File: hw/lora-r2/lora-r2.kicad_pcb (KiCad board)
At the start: 2 copper layers, 74 x 59 mm, 18 parts, among them J1 Conn_Coaxial, J2 SWD, J3 Conn_02x08_Odd_Even, J4 Conn_01x06, Q1 IRLML6401, U1 Pico_1_PCB, U3 MCP1700x-330xxTT

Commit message: Making progress on layout
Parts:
- removed C5: 10u, Capacitor_SMD:CP_Elec_4x5.4
- removed J4: Conn_01x06, Connector_PinHeader_2.54mm:PinHeader_1x06_P2.54mm_Vertical
- added C1: 10u, Capacitor_SMD:C_0805_2012Metric_Pad1.18x1.45mm_HandSolder, F.Cu at (80.0, 97.5)
- J3: value Conn_02x08_Odd_Even -> Conn_02x12_Odd_Even; footprint Connector_PinHeader_2.54mm:PinHeader_2x08_P2.54mm_Vertical -> Connector_PinHeader_2.54mm:PinHeader_2x12_P2.54mm_Vertical
- moved R4 56.5 mm to (73.5, 88.0)
- moved R5 56.5 mm to (73.5, 90.5)
- moved C2 56.2 mm to (80.0, 87.8), turned to 90 degrees
- moved U3 52.5 mm to (80.0, 93.9), turned to 90 degrees
- moved R1 50.2 mm to (80.0, 79.0)
- moved R2 50.2 mm to (80.0, 81.5)
- moved H3 16.0 mm to (122.0, 81.0)
- moved H4 16.0 mm to (122.0, 132.0)
- moved J2 3.58 mm to (102.9, 133.0)
- moved U1 3.50 mm to (105.6, 103.4)
- moved H1 2.83 mm to (72.0, 81.0)
- moved J3 1.39 mm to (86.0, 79.9)
- moved J1 1.08 mm to (73.5, 106.5)
- moved U2 0.70 mm to (87.6, 124.7)
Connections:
- C2 pad 1: VCONV -> VCON
- J3 pad 1: GPIO0 -> VPAN
- J3 pad 10: GPIO9 -> GPIO4
- J3 pad 11: VPAN_SENSE -> VCON_SENSE
- J3 pad 12: GPIO26 -> GPIO5
- J3 pad 13: VCON_SENSE -> GPIO27
- J3 pad 14: GPIO27 -> GPIO6
- J3 pad 15: GND -> VPAN_SENSE
- J3 pad 16: GND -> GPIO7
- J3 pad 2: GPIO1 -> GPIO0
- J3 pad 3: GPIO2 -> VPAN
- J3 pad 4: GPIO3 -> GPIO1
- J3 pad 5: GPIO4 -> VCON
- J3 pad 6: GPIO5 -> GPIO2
- J3 pad 7: GPIO6 -> +3.3V
- J3 pad 8: GPIO7 -> GPIO3
- J3 pad 9: GPIO8 -> GPIO26
- Q1 pad 1: GPIO20 -> GPIO15
- U1 pad 20: unconnected-(U1-GPIO15-Pad20) -> GPIO15
- U1 pad 26: GPIO20 -> unconnected-(U1-GPIO20-Pad26)
- U3 pad 2: +3V3 -> +3.3V
- U3 pad 3: VCONV -> VCON
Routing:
- net +3.3V: track 0.00 -> 32.7 mm
- net VCON: track 0.00 -> 17.5 mm
- net GPIO8: track 23.7 -> 10.0 mm
- net GPIO15: track 0.00 -> 11.9 mm
- net GPIO9: track 21.8 -> 10.0 mm
- net GPIO6: track 21.3 -> 10.0 mm
- net Net-(J1-In): track 0.00 -> 11.0 mm
- net GPIO7: track 19.8 -> 10.0 mm
- net GPIO4: track 18.1 -> 8.99 mm
- net GPIO2: track 17.0 -> 8.99 mm
- net VPAN: track 0.00 -> 7.88 mm
- net GPIO0: track 15.6 -> 8.70 mm
- net GPIO5: track 15.6 -> 8.99 mm
- net GPIO3: track 15.1 -> 8.99 mm
- net GPIO1: track 12.5 -> 8.50 mm
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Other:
- board size 74 x 59 mm -> 58 x 59 mm

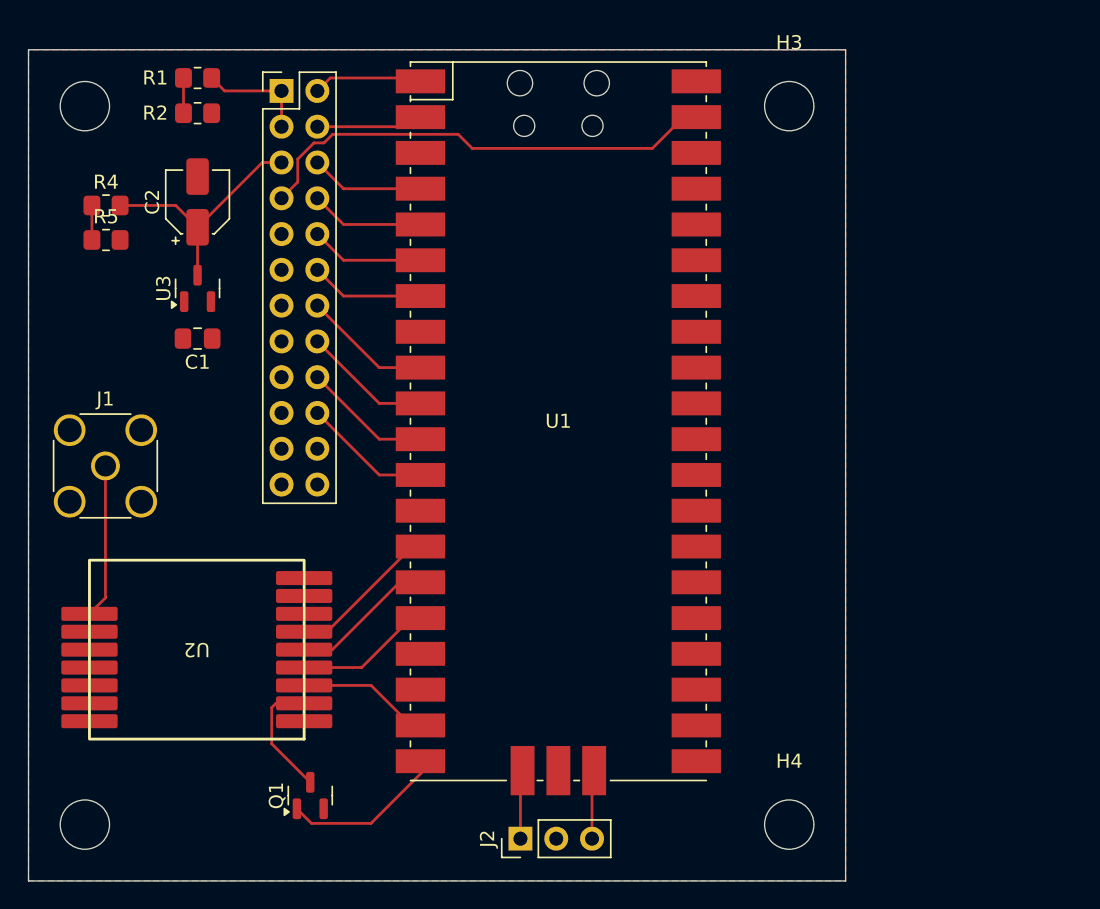
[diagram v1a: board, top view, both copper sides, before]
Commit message: First layout that passes DRC
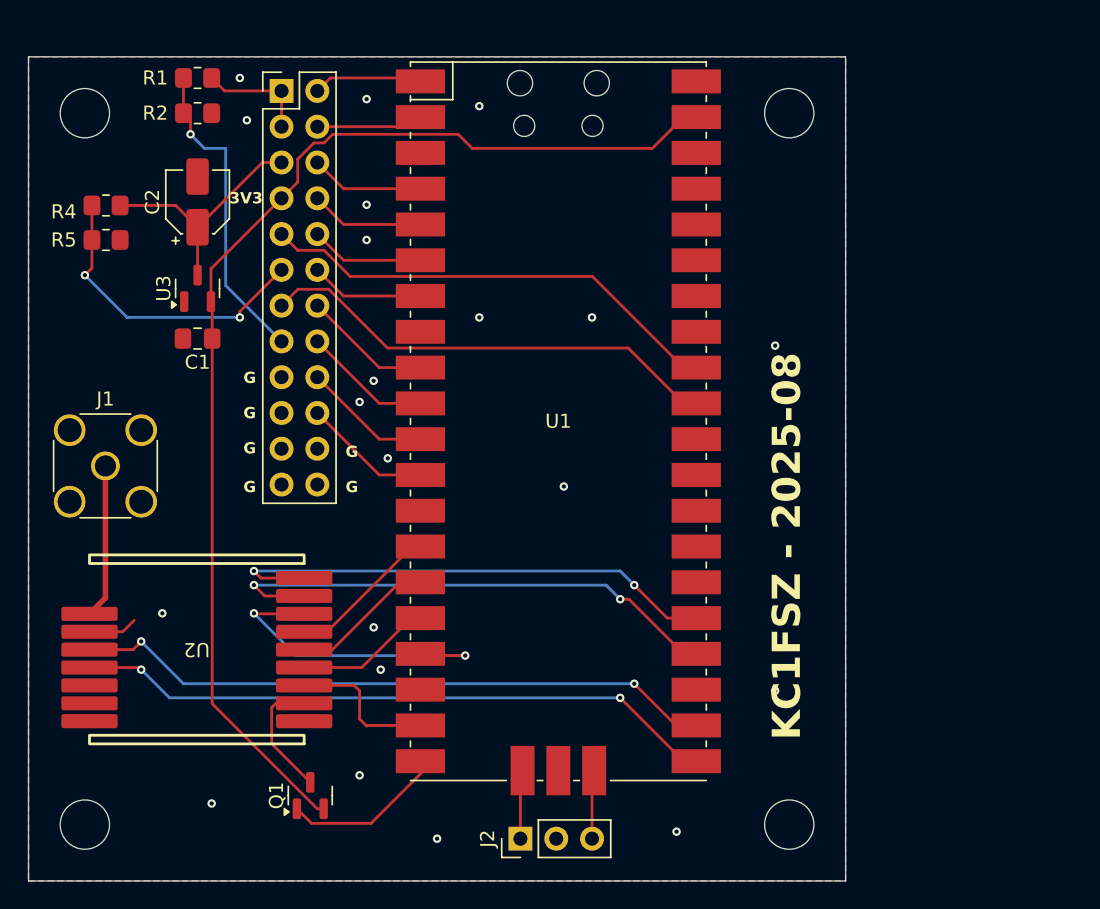
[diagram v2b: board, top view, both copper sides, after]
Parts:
- moved H1 0.50 mm to (72.0, 81.5)
- moved H3 0.50 mm to (122.0, 81.5)
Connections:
- net Net-(J1-In) renamed /Controller/ANT
- J3 pad 13: GPIO27 -> GPIO26
- J3 pad 9: GPIO26 -> GPIO27
- U1 pad 21: RADIO_RFSW_V1 -> RADIO_INT
- U1 pad 22: RADIO_RFSW_V2 -> RADIO_BUSY
- U1 pad 24: RADIO_BUSY -> RADIO_RFSW_V2
- U1 pad 25: RADIO_INT -> RADIO_RFSW_V1
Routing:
- net +3.3V: track 32.7 -> 81.7 mm
- net RADIO_INT: track 0.00 -> 44.9 mm, vias 0 -> 2
- net RADIO_BUSY: track 0.00 -> 44.9 mm, vias 0 -> 2
- net RADIO_RFSW_V2: track 0.00 -> 36.4 mm, vias 0 -> 2
- net RADIO_RFSW_V1: track 0.00 -> 35.7 mm, vias 0 -> 2
- net GPIO27: track 0.00 -> 32.5 mm
- net GPIO26: track 0.00 -> 32.4 mm
- net SPI_CS: track 0.00 -> 22.2 mm, vias 0 -> 2
- net VPAN_SENSE: track 2.50 -> 22.5 mm, vias 0 -> 1
- net VCON_SENSE: track 2.45 -> 22.0 mm, vias 0 -> 2
- net GND: track 0.00 -> 3.51 mm, vias 0 -> 21
- net ~{RADIO_RESET}: track 10.3 -> 11.5 mm
- added copper zone on B.Cu, net GND
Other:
- board size 58 x 59 mm -> 58 x 58.5 mm
- board text added: "3V3"
- board text added: "G"
- board text added: "KC1FSZ - 2025-08"

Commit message: Generated first Gerbers
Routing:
- net GND: vias 21 -> 36
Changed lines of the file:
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@@
 		(legacy_teardrops no)
 	)
-	(paper "A4")
+	(paper "USLetter")
+	(title_block
+		(title "KC1FSZ LoRa Controller Board")
+		(date "2025-05-08")
+		(rev "1")
+		(company "Bruce MacKinnon")
+		(comment 1 "Copyright (C) 2025, Bruce MacKinnon")
+		(comment 2 "NOT FOR COMMERCIAL USE")
+	)
 	(layers
 		(0 "F.Cu" signal)
@@
 			(plot_on_all_layers_selection 0x00000000_00000000_00000000_00000000)
 			(disableapertmacros no)
-			(usegerberextensions no)
-			(usegerberattributes yes)
-			(usegerberadvancedattributes yes)
-			(creategerberjobfile yes)
+			(usegerberextensions yes)
+			(usegerberattributes no)
+			(usegerberadvancedattributes no)
+			(creategerberjobfile no)
 			(dashed_line_dash_ratio 12.000000)
 			(dashed_line_gap_ratio 3.000000)
@@
 			(psa4output no)
 			(plot_black_and_white yes)
-			(plotinvisibletext no)
+			(plotinvisibletext yes)
 			(sketchpadsonfab no)
 			(plotpadnumbers no)
@@
 			(sketchdnponfab yes)
 			(crossoutdnponfab yes)
-			(subtractmaskfromsilk no)
+			(subtractmaskfromsilk yes)
 			(outputformat 1)
 			(mirror no)
-			(drillshape 1)
+			(drillshape 0)
 			(scaleselection 1)
-			(outputdirectory "")
+			(outputdirectory "plots")
 		)
 	)
@@
 	)
 	(via
+		(at 75.75 116.5)
+		(size 0.6)
+		(drill 0.3)
+		(layers "F.Cu" "B.Cu")
+		(free yes)
+		(net 1)
+	)
+	(via
 		(at 92 80.5)
 		(size 0.6)
@@
 	)
 	(via
+		(at 75.75 106.5)
+		(size 0.6)
+		(drill 0.3)
+		(layers "F.Cu" "B.Cu")
+		(free yes)
+		(net 1)
+	)
+	(via
+		(at 71.75 115.25)
+		(size 0.6)
+		(drill 0.3)
+		(layers "F.Cu" "B.Cu")
+		(free yes)
+		(net 1)
+	)
+	(via
 		(at 91.5 128.5)
 		(size 0.6)
@@
 	)
 	(via
+		(at 79.25 106.5)
+		(size 0.6)
+		(drill 0.3)
+		(layers "F.Cu" "B.Cu")
+		(free yes)
+		(net 1)
+	)
+	(via
 		(at 100 96)
 		(size 0.6)
@@
 	)
 	(via
+		(at 72 111.25)
+		(size 0.6)
+		(drill 0.3)
+		(layers "F.Cu" "B.Cu")
+		(free yes)
+		(net 1)
+	)
+	(via
 		(at 121 98)
 		(size 0.6)
@@
 	)
 	(via
+		(at 76.25 100.5)
+		(size 0.6)
+		(drill 0.3)
+		(layers "F.Cu" "B.Cu")
+		(free yes)
+		(net 1)
+	)
+	(via
+		(at 75 113)
+		(size 0.6)
+		(drill 0.3)
+		(layers "F.Cu" "B.Cu")
+		(free yes)
+		(net 1)
+	)
+	(via
+		(at 75 115)
+		(size 0.6)
+		(drill 0.3)
+		(layers "F.Cu" "B.Cu")
+		(free yes)
+		(net 1)
+	)
+	(via
 		(at 92.5 100.5)
 		(size 0.6)
@@
 	)
 	(via
+		(at 87 110.75)
+		(size 0.6)
+		(drill 0.3)
+		(layers "F.Cu" "B.Cu")
+		(free yes)
+		(net 1)
+	)
+	(via
+		(at 73.5 104)
+		(size 0.6)
+		(drill 0.3)
+		(layers "F.Cu" "B.Cu")
+		(free yes)
+		(net 1)
+	)
+	(via
+		(at 71.25 100)
+		(size 0.6)
+		(drill 0.3)
+		(layers "F.Cu" "B.Cu")
+		(free yes)
+		(net 1)
+	)
+	(via
 		(at 106 108)
 		(size 0.6)
@@
 	)
 	(via
+		(at 71 113.75)
+		(size 0.6)
+		(drill 0.3)
+		(layers "F.Cu" "B.Cu")
+		(free yes)
+		(net 1)
+	)
+	(via
+		(at 72 113)
+		(size 0.6)
+		(drill 0.3)
+		(layers "F.Cu" "B.Cu")
+		(free yes)
+		(net 1)
+	)
+	(via
+		(at 75 111.25)
+		(size 0.6)
+		(drill 0.3)
+		(layers "F.Cu" "B.Cu")
+		(free yes)
+		(net 1)
+	)
+	(via
 		(at 92 90.5)
 		(size 0.6)
@@
 		(size 0.6)
 		(drill 0.3)
+		(layers "F.Cu" "B.Cu")
+		(free yes)
+		(net 1)
+	)
+	(via
+		(at 71 106.5)
+		(size 0.6)
+		(drill 0.3)

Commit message: Ready for fabrication
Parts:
- moved J3 1.50 mm to (86.0, 81.4)
- moved R1 1.25 mm to (80.0, 80.2)
- moved R2 1.25 mm to (80.0, 82.8)
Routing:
- net VPAN_SENSE: track 22.5 -> 28.4 mm, vias 1 -> 2
- net GPIO1: track 8.50 -> 10.1 mm
- net GPIO0: track 8.70 -> 9.58 mm
- net VCON_SENSE: track 22.0 -> 21.1 mm
- net +3.3V: track 81.7 -> 82.5 mm
- net VCON: track 17.5 -> 16.8 mm
- net GPIO9: track 10.0 -> 9.42 mm
- net GPIO8: track 10.0 -> 9.42 mm
- net GPIO6: track 10.0 -> 9.42 mm
- net GPIO5: track 8.99 -> 8.37 mm
- net GPIO4: track 8.99 -> 8.37 mm
- net GPIO2: track 8.99 -> 8.37 mm
- net GPIO7: track 10.0 -> 9.42 mm
- net GPIO3: track 8.99 -> 8.37 mm
- net GPIO27: track 32.5 -> 31.8 mm
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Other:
- board text added: "SWCLK"
- board text added: "SWDIO"

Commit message: SENT TO FAB (2025-05-08 13:04)
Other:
- board text added: "CO"
- board text added: "PA"
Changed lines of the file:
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@@
 		)
 		(embedded_fonts no)
-		(model "C:/Users/ncara/OneDrive/IoT/Tools/KiCad/RP-Pico Libraries/Pico.wrl"
+		(model "C:/git/kicad-library/3d/Pico-R3.step"
 			(offset
-				(xyz 0 0 0)
+				(xyz -10.5 -25.5 0)
 			)
 			(scale
@@
 			)
 			(rotate
-				(xyz 0 0 0)
+				(xyz -90 -0 -0)
 			)
 		)
@@
 		)
 	)
+	(gr_text "CO"
+		(at 82.7 87 0)
+		(layer "F.SilkS")
+		(effects
+			(font
+				(size 0.8 0.8)
+				(thickness 0.15)
+				(bold yes)
+			)
+			(justify left bottom)
+		)
+	)
 	(gr_text "3V3"
 		(at 82.25 89.5 0)
@@
 		)
 	)
+	(gr_text "PA"
+		(at 82.8 82 0)
+		(layer "F.SilkS")
+		(effects
+			(font
+				(size 0.8 0.8)
+				(thickness 0.15)
+				(bold yes)
+			)
+			(justify left bottom)
+		)
+	)
 	(gr_text "SWCLK"
 		(at 95.75 133.5 0)
@@
 			)
 			(justify left bottom)
+		)
+	)
+	(gr_text "PA"
+		(at 82.7 84.5 0)
+		(layer "F.SilkS")
+		(effects
+			(font
+				(size 0.8 0.8)
+				(thickness 0.15)
+				(bold yes)
+			)
+			(justify left bottom)

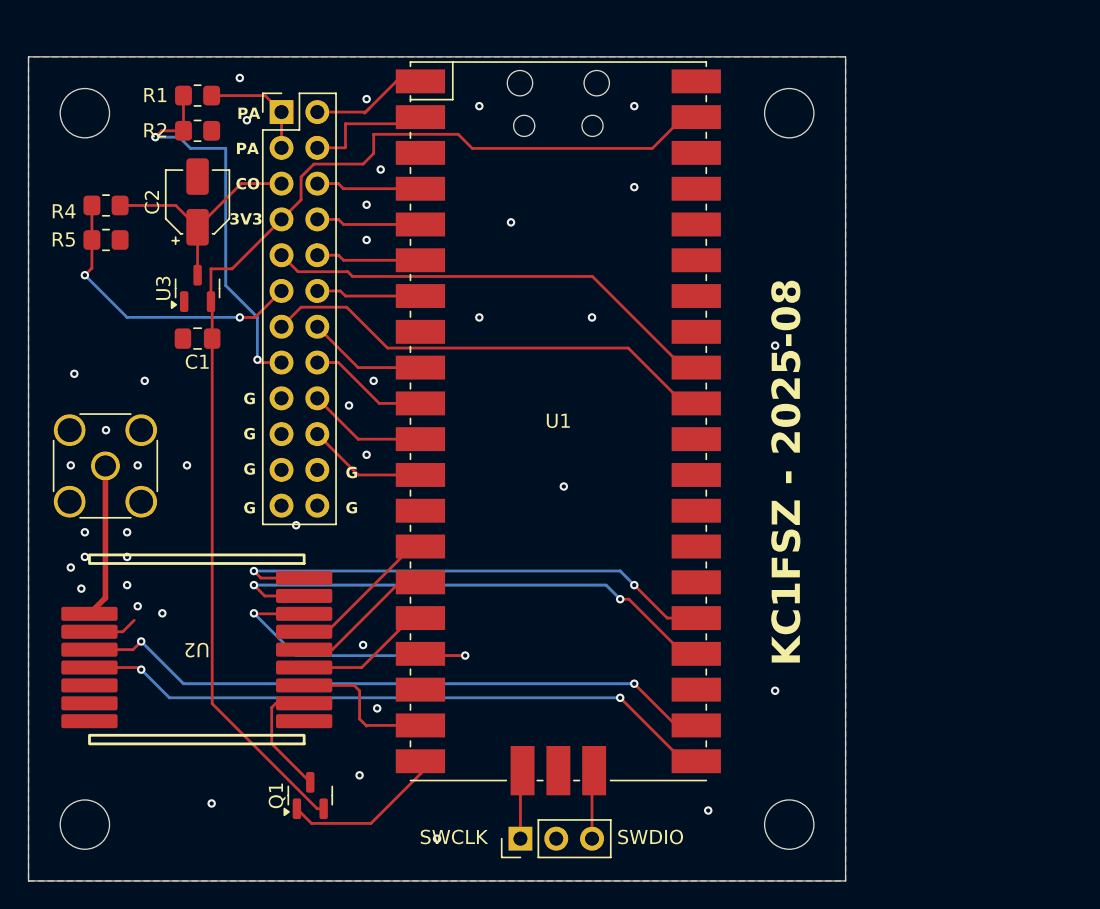
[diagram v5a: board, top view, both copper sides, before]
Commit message: Revision (before fab) - can power radio from USB now
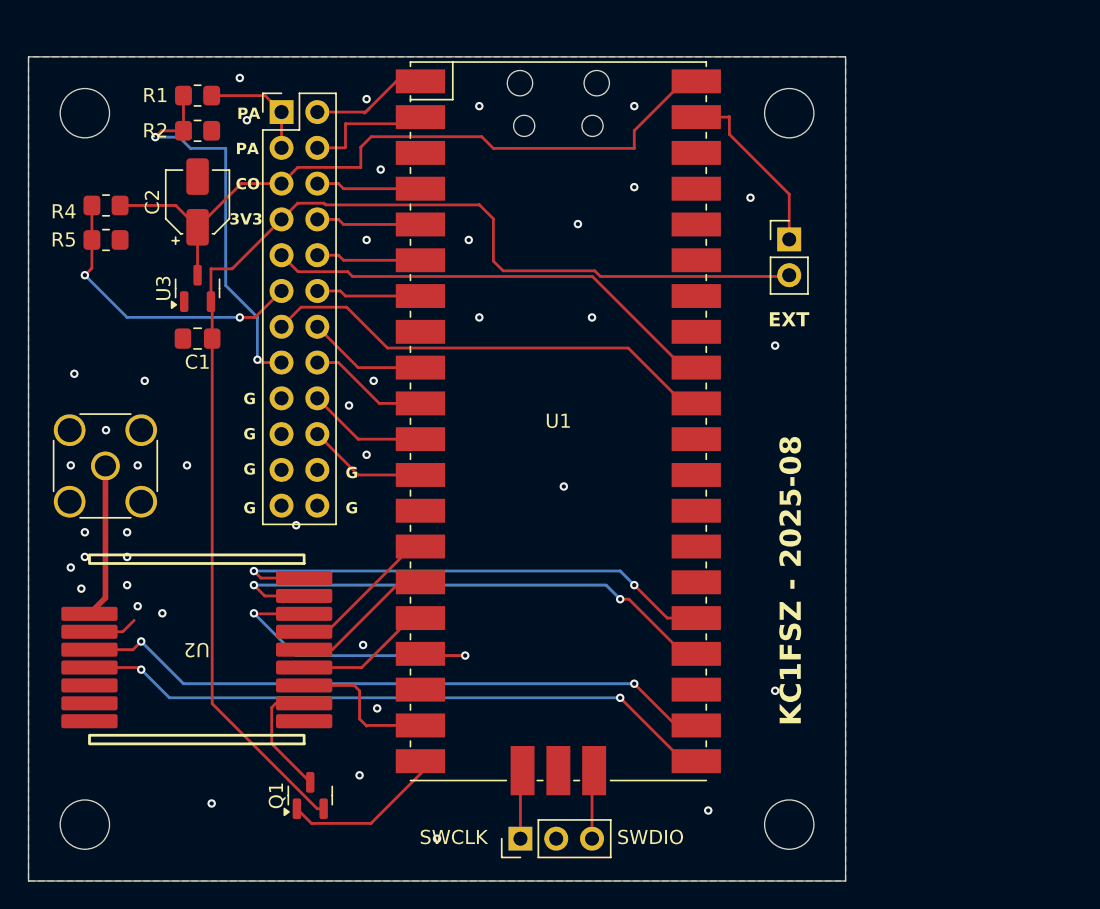
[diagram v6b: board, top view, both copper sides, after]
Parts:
- added J4: E3, Connector_PinHeader_2.54mm:PinHeader_1x02_P2.54mm_Vertical, F.Cu at (122.0, 90.5)
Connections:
- U1 pad 39: +3.3V -> Net-(J4-Pin_1)
- U1 pad 40: unconnected-(U1-VBUS-Pad40) -> VCON
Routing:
- net VCON: track 16.8 -> 50.6 mm
- net Net-(J4-Pin_1): track 0.00 -> 13.7 mm
- net +3.3V: track 82.5 -> 88.8 mm
- net GND: vias 40 -> 41
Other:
- board text added: "EXT"
